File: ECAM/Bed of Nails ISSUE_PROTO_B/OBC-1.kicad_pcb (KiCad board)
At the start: 6 copper layers, 42.8 x 42.8 mm, 43 parts, among them J1 ERF8-020-X, J2 MTSW-X20

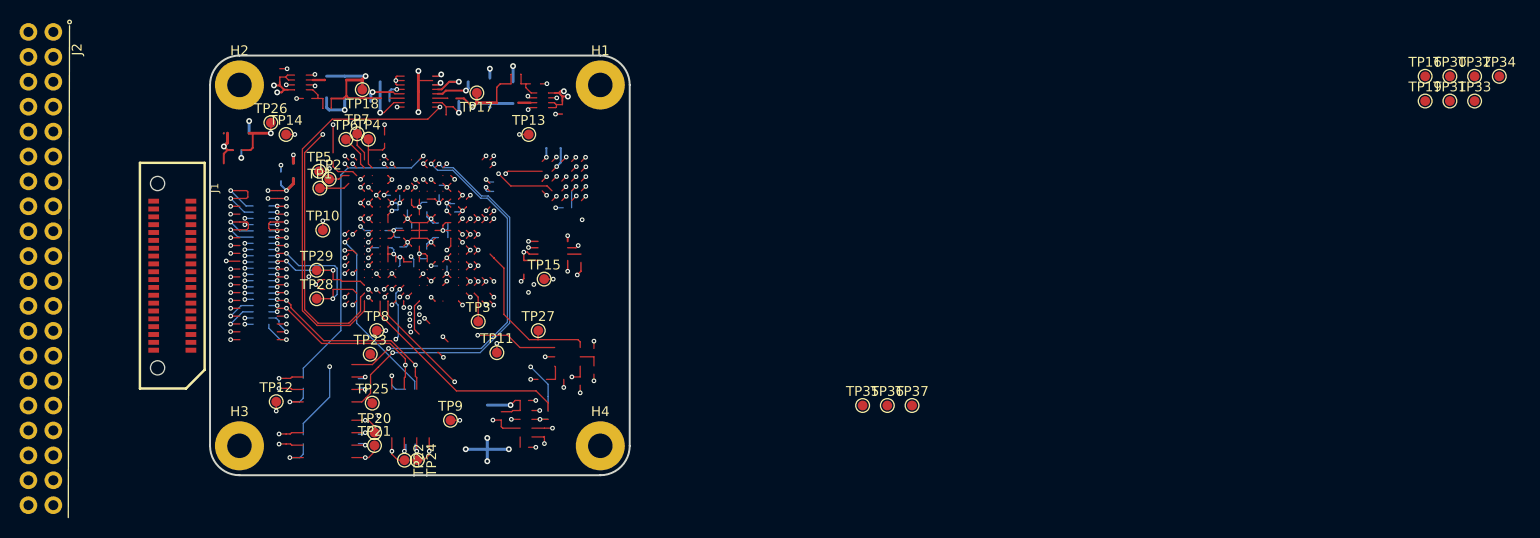
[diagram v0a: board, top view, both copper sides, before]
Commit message: updating PCB with current proto_B test point locations
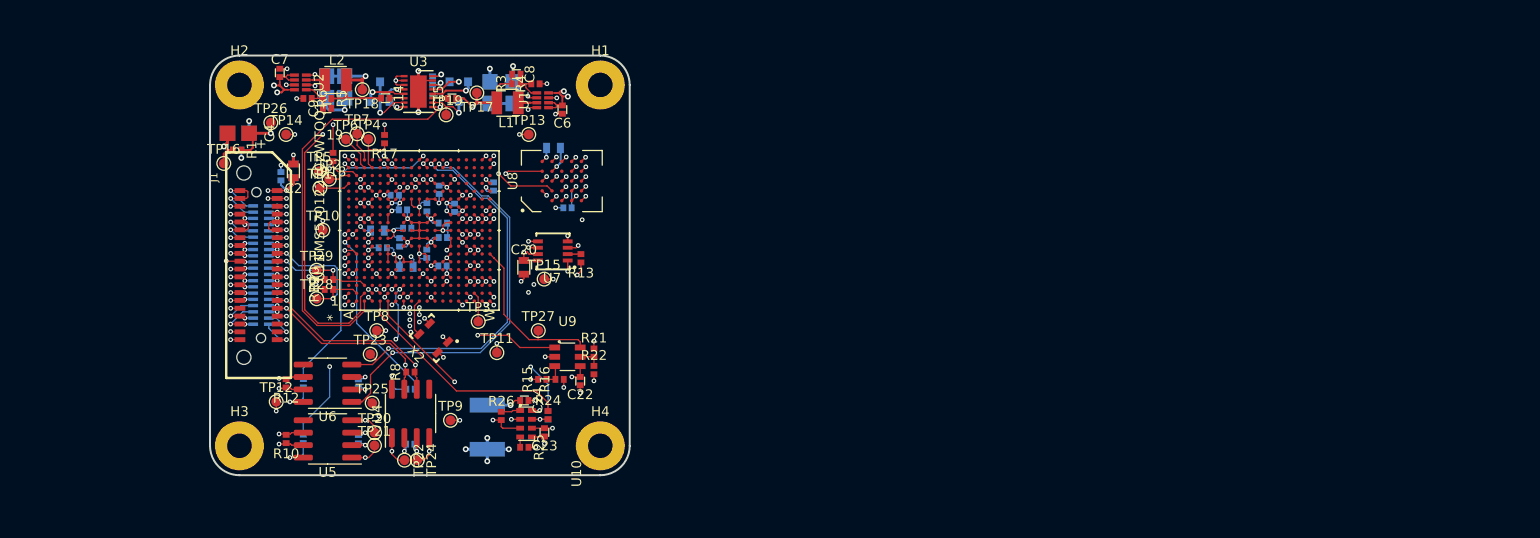
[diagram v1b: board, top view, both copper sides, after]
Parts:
- removed TP30, TP31, TP32, TP33, TP34, TP35, TP36, TP37: TEST-POINT, TFT_TestPoints:TP_RDPad_D1.0mm
- added C1: 100n-10V-0402-5%-CER, TFT_C_passive_SMD:0402_CAP, B.Cu at (96.1, 83.8)
- added C10: 10u-10V-0603-10%-CER, TFT_C_passive_SMD:1206_CAP_TANT, B.Cu at (119.8, 75.3)
- added C11: 10u-10V-0603-10%-CER, TFT_C_passive_SMD:1206_CAP_TANT, B.Cu at (100.8, 74.7)
- added C12: 10u-10V-0603-10%-CER, TFT_C_passive_SMD:1206_CAP_TANT, B.Cu at (117.4, 75.3)
- added C13: 10u-10V-0603-10%-CER, TFT_C_passive_SMD:1206_CAP_TANT, B.Cu at (102.6, 74.7)
- added C14: 56n-16V-0402-10%-CER, TFT_C_passive_SMD:0402_CAP, F.Cu at (106.8, 75.8)
- added C15: 56n-16V-0402-10%-CER, TFT_C_passive_SMD:0402_CAP, F.Cu at (113.6, 75.9)
- added C16: 100n-10V-0402-5%-CER, TFT_C_passive_SMD:0402_CAP, B.Cu at (111.6, 74.1)
- added C17: 100n-10V-0402-5%-CER, TFT_C_passive_SMD:0402_CAP, B.Cu at (109.3, 111.1)
- added C18: 100n-10V-0402-5%-CER, TFT_C_passive_SMD:0402_CAP, B.Cu at (104.0, 110.6)
- added C19: 100n-10V-0402-5%-CER, TFT_C_passive_SMD:0402_CAP, B.Cu at (104.0, 104.9)
- added C2: 1u-10V-0603-10%-CER, TFT_C_passive_SMD:0603_CAP, F.Cu at (97.4, 83.3)
- added C20: 100n-10V-0402-5%-CER, TFT_C_passive_SMD:0603_CAP, F.Cu at (120.9, 93.1)
- added C21: 100n-10V-0402-5%-CER, TFT_C_passive_SMD:0603_CAP, B.Cu at (123.9, 80.9)
- added C22: 100n-10V-0402-5%-CER, TFT_C_passive_SMD:0402_CAP, F.Cu at (126.7, 104.7)
- added C23: 100n-10V-0402-5%-CER, TFT_C_passive_SMD:0402_CAP, F.Cu at (123.0, 109.9)
- added C24: 100n-10V-0402-5%-CER, TFT_C_passive_SMD:0402_CAP, F.Cu at (120.9, 106.7)
- added C25: 100uAH-1V8-4.4x3mm_LIon_batt, TFT_misc:1812_BATT, B.Cu at (117.2, 109.4)
- added C28: 1u-10V-0603-10%-CER, TFT_C_passive_SMD:0603_CAP, B.Cu at (108.9, 93.0)
- added C29: 1u-10V-0603-10%-CER, TFT_C_passive_SMD:0603_CAP, B.Cu at (106.0, 89.3)
- added C3: 1u-10V-0603-10%-CER, TFT_C_passive_SMD:0603_CAP, B.Cu at (97.4, 83.3)
- added C30: 100n-10V-0402-5%-CER, TFT_C_passive_SMD:0402_CAP, B.Cu at (108.5, 87.2)
- added C31: 100n-10V-0402-5%-CER, TFT_C_passive_SMD:0402_CAP, B.Cu at (112.3, 85.2)
- added C32: 100n-10V-0402-5%-CER, TFT_C_passive_SMD:0402_CAP, B.Cu at (109.0, 89.1)
- added C33: 100n-10V-0402-5%-CER, TFT_C_passive_SMD:0402_CAP, B.Cu at (112.7, 90.1)
- added C34: 100n-10V-0402-5%-CER, TFT_C_passive_SMD:0402_CAP, B.Cu at (106.5, 91.1)
- added C35: 100n-10V-0402-5%-CER, TFT_C_passive_SMD:0402_CAP, B.Cu at (107.8, 85.7)
- added C36: 100n-10V-0402-5%-CER, TFT_C_passive_SMD:0402_CAP, B.Cu at (112.7, 88.6)
- added C37: 100n-10V-0402-5%-CER, TFT_C_passive_SMD:0402_CAP, B.Cu at (108.2, 90.5)
- added C38: 100n-10V-0402-5%-CER, TFT_C_passive_SMD:0402_CAP, B.Cu at (112.6, 93.0)
- added C39: 100n-10V-0402-5%-CER, TFT_C_passive_SMD:0402_CAP, B.Cu at (113.8, 87.0)
- added C4: 10u-10V-1206-10%-TANT, TFT_C_passive_SMD:1206_CAP_TANT, F.Cu at (91.8, 79.4)
- added C40: 100n-10V-0402-5%-CER, TFT_C_passive_SMD:0402_CAP, B.Cu at (111.0, 86.9)
- added C41: 100n-10V-0402-5%-CER, TFT_C_passive_SMD:0402_CAP, B.Cu at (111.0, 91.7)
- added C42: 100n-10V-0402-5%-CER, TFT_C_passive_SMD:0402_CAP, B.Cu at (117.8, 84.9)
- added C5: 10u-10V-1206-10%-TANT, TFT_C_passive_SMD:1206_CAP_TANT, B.Cu at (91.8, 79.4)
- added C6: 100n-10V-0402-5%-CER, TFT_C_passive_SMD:0402_CAP, F.Cu at (124.8, 77.0)
- added C7: 100n-10V-0402-5%-CER, TFT_C_passive_SMD:0402_CAP, F.Cu at (96.0, 73.3)
- added C8: 10p-50V-0402-0.5p-CER, TFT_C_passive_SMD:0402_CAP, F.Cu at (120.1, 73.4)
- added C9: 10p-50V-0402-0.5p-CER, TFT_C_passive_SMD:0402_CAP, F.Cu at (100.9, 76.9)
- added L1: 470nH-4A-20%, TFT_I_passive_SMD:2.5x2mm_I_SMD, F.Cu at (119.2, 76.3)
- added L2: 470nH-4A-20%, TFT_I_passive_SMD:2.5x2mm_I_SMD, F.Cu at (101.7, 74.0)
- added Q1: MGSF1N02L, Package_TO_SOT_SMD:SOT-23, B.Cu at (106.2, 75.2)
- added Q2: MGSF1N02L, Package_TO_SOT_SMD:SOT-23, B.Cu at (114.3, 75.2)
- added R1: 100K-50V-0402-1%, TFT_R_passive_SMD:0402_RES, F.Cu at (91.7, 81.1)
- added R10: 120R-50V-0402-1%, TFT_R_passive_SMD:0402_RES, F.Cu at (96.7, 110.6)
- added R11: 10K-50V-0402-1%, TFT_R_passive_SMD:0402_RES, B.Cu at (98.4, 104.9)
- added R12: 120R-50V-0402-1%, TFT_R_passive_SMD:0402_RES, F.Cu at (96.7, 104.9)
- added R13: 39R0-50V-0402-1%, TFT_R_passive_SMD:0402_RES, F.Cu at (126.7, 92.2)
- added R14: 39R0-50V-0402-1%, TFT_R_passive_SMD:0402_RES, B.Cu at (125.3, 87.0)
- added R15: 0R-50V-0402, TFT_R_passive_SMD:0402_RES, F.Cu at (122.8, 104.5)
- added R16: 0R-50V-0402, TFT_R_passive_SMD:0402_RES, F.Cu at (124.5, 104.5)
- added R17: 4K7-50V-0402-1%, TFT_R_passive_SMD:0402_RES, F.Cu at (106.7, 80.0)
- added R18: 4K7-50V-0402-1%, TFT_R_passive_SMD:0402_RES, F.Cu at (101.5, 81.8)
- added R19: 4K7-50V-0402-1%, TFT_R_passive_SMD:0402_RES, F.Cu at (101.0, 95.3)
- added R2: 100K-50V-0402-1%, TFT_R_passive_SMD:0402_RES, B.Cu at (91.7, 81.1)
- added R20: 4K7-50V-0402-1%, TFT_R_passive_SMD:0402_RES, F.Cu at (101.0, 94.3)
- added R21: 0R-50V-0402, TFT_R_passive_SMD:0402_RES, F.Cu at (128.1, 101.8)
- added R22: 0R-50V-0402, TFT_R_passive_SMD:0402_RES, F.Cu at (128.1, 103.6)
- added R23: 0R-50V-0402, TFT_R_passive_SMD:0402_RES, B.Cu at (123.4, 108.2)
- added R24: 0R-50V-0402, TFT_R_passive_SMD:0402_RES, F.Cu at (123.4, 108.2)
- added R25: 10K-50V-0402-1%, TFT_R_passive_SMD:0402_RES, F.Cu at (121.0, 111.5)
- added R26: 10K-50V-0402-1%, TFT_R_passive_SMD:0402_RES, F.Cu at (118.6, 108.2)
- added R3: 16K2-50V-0402-1%, TFT_R_passive_SMD:0402_RES, F.Cu at (120.1, 74.4)
- added R4: 15K-50V-0402-1%, TFT_R_passive_SMD:0402_RES, F.Cu at (122.1, 74.4)
- added R5: 16K2-50V-0402-1%, TFT_R_passive_SMD:0402_RES, F.Cu at (100.8, 75.9)
- added R6: 15K-50V-0402-1%, TFT_R_passive_SMD:0402_RES, F.Cu at (98.8, 75.9)
- added R7: 10K-50V-0402-1%, TFT_R_passive_SMD:0402_RES, B.Cu at (109.4, 105.5)
- added R8: 120R-50V-0402-1%, TFT_R_passive_SMD:0402_RES, F.Cu at (109.3, 103.8)
- added R9: 10K-50V-0402-1%, TFT_R_passive_SMD:0402_RES, B.Cu at (98.4, 110.6)
- added U1: TPS62850x-Q1, TFT_SOT:SOT-583, F.Cu at (123.4, 76.8)
- added U10: RV-3032-C7, TFT_misc:RV-3032-C7, F.Cu at (121.1, 109.0)
- added U11: TMS5701227CZWTQQ1, TFT_BGA:ZWT337, F.Cu at (110.2, 89.3)
- added U2: TPS62850x-Q1, TFT_SOT:SOT-583, F.Cu at (97.5, 73.5)
- added U3: LTC4353, Package_DFN_QFN:DFN-16-1EP_3x4mm_P0.45mm_EP1.7x3.3mm, F.Cu at (110.2, 75.2)
- added U4: SN65HVD230M-EP, Package_SO:SOIC-8_3.9x4.9mm_P1.27mm, F.Cu at (109.3, 108.0)
- added U5: SN65HVD230M-EP, Package_SO:SOIC-8_3.9x4.9mm_P1.27mm, F.Cu at (100.9, 110.6)
- added U6: SN65HVD230M-EP, Package_SO:SOIC-8_3.9x4.9mm_P1.27mm, F.Cu at (100.9, 104.9)
- added U7: CY15B108QI, TFT_GQFN:CY15B108QI, F.Cu at (125.4, 92.4)
- added U8: S70FL01GS, TFT_BGA:BGA-24_5x5_6.0x8.0mm, F.Cu at (124.8, 84.3)
- added U9: TPS3813K33-EP, TFT_SOT:SOT-236, F.Cu at (125.3, 102.2)
- added X2: LFTCXO075797, TFT_XTAL:LFTCXO075797, F.Cu at (113.2, 100.7)
- J1: value ERF8-020-X -> ERM8-020-X; footprint TFT_connectors:ERF8-020-XX.X-X-DV -> TFT_connectors:ERM8-020-XX.X-X-DV
- J2: value MTSW-X20 -> ERF6-020-X; footprint TFT_connectors:MSTW-120-08-D-160-RA -> TFT_connectors:ERF6-020-XX.X-X-DV-A-XX-K; moved to B.Cu
- moved TP16 122.8 mm to (90.3, 82.5)
- moved TP19 99.9 mm to (113.0, 77.5)
- moved J2 22.5 mm to (94.1, 92.9)
- moved J1 8.87 mm to (93.8, 92.9)
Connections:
- J1 pad 10: /TMS570_uC/OBC_I2C_SCL -> /RTC/OBC_I2C_SCL
- J1 pad 15: /Connectors/CAN_L_PL -> /CAN_XCVR_PL/CAN_L_PL
- J1 pad 16: /Connectors/CAN_H_PL -> /CAN_XCVR_PL/CAN_H_PL
- J1 pad 19: /Connectors/CAN_H_R -> /CAN_XCVR_R/CAN_H_PL
- J1 pad 20: /Connectors/CAN_L_R -> /CAN_XCVR_R/CAN_L_PL
- J1 pad 9: /TMS570_uC/OBC_I2C_SDA -> /RTC/OBC_I2C_SDA
- J2 pad 1: OBC_3V3 -> GND
- J2 pad 10: /CAN_R_R -> GND
- J2 pad 12: /OBC_1V25_P_PG -> GND
- J2 pad 13: /OBC_1V25_R_PG -> GND
- J2 pad 14: /OBC_1V25_P -> GND
- J2 pad 15: /OBC_1V25_R -> GND
- J2 pad 16: /OBC_1V25 -> GND
- J2 pad 17: Net-(J2-Pad17) -> GND
- J2 pad 18: Net-(J2-Pad18) -> GND
- J2 pad 19: Net-(J2-Pad19) -> /CAN_XCVR_R/CAN_H_PL
- J2 pad 2: OBC_3V3 -> GND
- J2 pad 20: Net-(J2-Pad20) -> /CAN_XCVR_R/CAN_L_PL
- J2 pad 21: /Connectors/CAN_L_PA -> GND
- J2 pad 22: /Connectors/CAN_H_PA -> GND
- J2 pad 23: GND -> /Connectors/CAN_L_PA
- J2 pad 24: GND -> /Connectors/CAN_H_PA
- J2 pad 25: /Connectors/CAN_L_PL -> GND
- J2 pad 26: /Connectors/CAN_H_PL -> GND
- J2 pad 29: /Connectors/CAN_H_R -> GND
- J2 pad 3: /CAN_PL_D -> GND
- J2 pad 30: /Connectors/CAN_L_R -> GND
- J2 pad 32: /TMS570_uC/OBC_I2C_SDA -> GND
- J2 pad 33: /TMS570_uC/OBC_I2C_SCL -> GND
- J2 pad 34: /Connectors/ADS_nRST -> GND
- J2 pad 35: GND -> PAYLOAD_3V3
- J2 pad 36: /Connectors/GPS_STS -> PAYLOAD_3V3
- J2 pad 37: /Connectors/GPS_P1PPS -> GND
- J2 pad 38: /Connectors/GPS_nRST -> GND
- J2 pad 39: /Connectors/GPS_RXD0 -> PAYLOAD_5V
- J2 pad 4: /CAN_PL_R -> GND
- J2 pad 40: /Connectors/GPS_TXD0 -> PAYLOAD_5V
- J2 pad 6: /CAN_PA_D -> GND
- J2 pad 7: /CAN_PA_R -> GND
- J2 pad 9: /CAN_R_D -> GND
- TP1 pad 1: /JTAG_RTCK -> /TMS570_uC/JTAG_RTCK
- TP16 pad 1: /Connectors/ADS_nRST -> Net-(C4-Pad2)
- TP17 pad 1: /OBC_1V25_P -> OBC_1V25_P
- TP18 pad 1: /OBC_1V25_R -> OBC_1V25_R
- TP19 pad 1: /Connectors/CAN_H_PL -> OBC_1V25
- TP2 pad 1: /JTAG_TDI -> /TMS570_uC/JTAG_TDI
- TP20 pad 1: /CAN_R_R -> /CAN_XCVR_R/CAN_PL_R
- TP21 pad 1: /CAN_R_D -> /CAN_XCVR_R/CAN_PL_D
- TP22 pad 1: /CAN_PL_D -> /CAN_XCVR_PL/CAN_PL_D
- TP23 pad 1: /CAN_PA_R -> /TMS570_uC/CAN_PA_R
- TP24 pad 1: /CAN_PL_R -> /CAN_XCVR_PL/CAN_PL_R
- TP25 pad 1: /CAN_PA_D -> /TMS570_uC/CAN_PA_D
- TP26 pad 1: /TMS570_uC/uC_nRST -> OBC_3V3
- TP27 pad 1: /SPVSR_nRST -> /Supervisor/SPVSR_nRST
- TP28 pad 1: /TMS570_uC/OBC_I2C_SDA -> /RTC/OBC_I2C_SDA
- TP29 pad 1: /TMS570_uC/OBC_I2C_SCL -> /RTC/OBC_I2C_SCL
- TP3 pad 1: /JTAG_TEST -> /TMS570_uC/JTAG_TEST
- TP4 pad 1: /JTAG_nTRST -> /TMS570_uC/JTAG_nTRST
- TP5 pad 1: /JTAG_TCK -> /TMS570_uC/JTAG_TCK
- TP6 pad 1: /JTAG_TDO -> /TMS570_uC/JTAG_TDO
- TP7 pad 1: /JTAG_TMS -> /TMS570_uC/JTAG_TMS
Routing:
- net /TMS570_uC/uC_nRST: track 113.7 -> 3.33 mm, vias 37 -> 0
- net OBC_3V3: track 0.00 -> 110.4 mm, vias 0 -> 37
- net /TMS570_uC/OBC_I2C_SCL: track 54.0 -> 0.00 mm, vias 3 -> 0
- net /RTC/OBC_I2C_SCL: track 0.00 -> 54.0 mm, vias 0 -> 3
- net /TMS570_uC/OBC_I2C_SDA: track 51.4 -> 0.00 mm, vias 3 -> 0
- net /RTC/OBC_I2C_SDA: track 0.00 -> 51.4 mm, vias 0 -> 3
- net /TMS570_uC/CAN_PA_D: track 0.00 -> 42.2 mm, vias 0 -> 2
- net /CAN_PA_D: track 42.2 -> 0.00 mm, vias 2 -> 0
- net /TMS570_uC/CAN_PA_R: track 0.00 -> 39.9 mm, vias 0 -> 2
- net /CAN_PA_R: track 39.9 -> 0.00 mm, vias 2 -> 0
- net /CAN_XCVR_PL/CAN_PL_R: track 0.00 -> 29.1 mm, vias 0 -> 2
- net /CAN_PL_R: track 29.1 -> 0.00 mm, vias 2 -> 0
- net /CAN_XCVR_PL/CAN_PL_D: track 0.00 -> 27.9 mm, vias 0 -> 2
- net /CAN_PL_D: track 27.9 -> 0.00 mm, vias 2 -> 0
- net /CAN_XCVR_R/CAN_PL_D: track 0.00 -> 21.6 mm, vias 0 -> 3
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
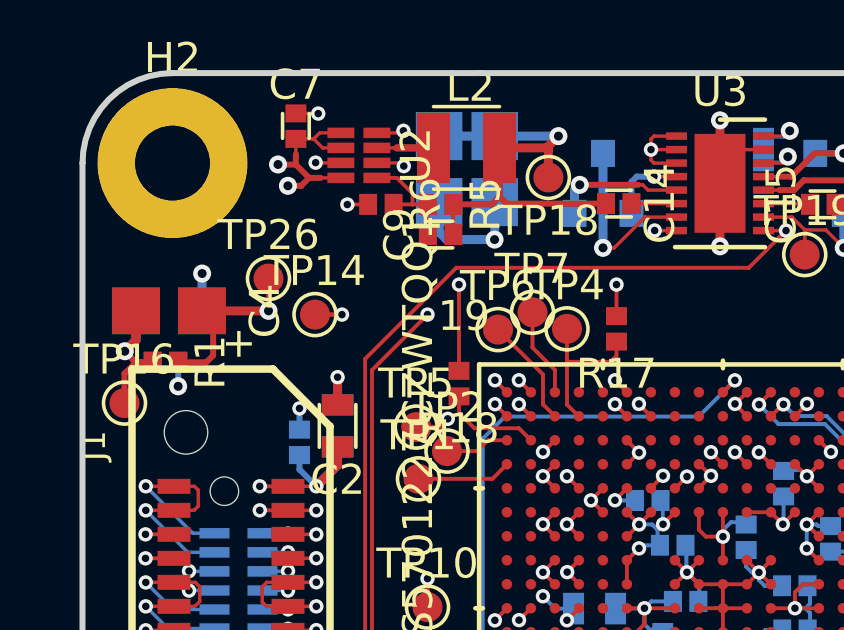
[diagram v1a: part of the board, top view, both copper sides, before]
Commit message: further PCB update to locate test points with current issue B PCB
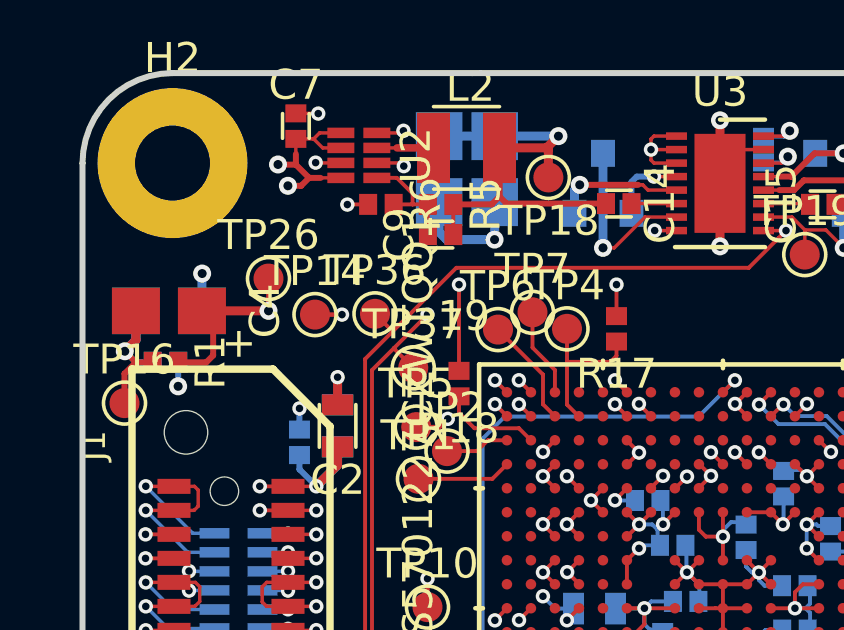
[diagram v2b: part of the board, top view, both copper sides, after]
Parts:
- added TP36: TEST-POINT, TFT_TestPoints:TP_RDPad_D1.0mm, F.Cu at (98.7, 79.5)
- added TP37: TEST-POINT, TFT_TestPoints:TP_RDPad_D1.0mm, F.Cu at (99.9, 81.3)
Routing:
- net /Power/OBC_1V25_R_PG: track 36.9 -> 37.8 mm
- net /Power/OBC_1V25_P_PG: track 41.6 -> 42.4 mm
